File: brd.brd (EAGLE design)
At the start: 40.3 x 62.2 mm, 15 parts, among them IC1 OP27Z, X1 BNC-H, X2 BNC-H, X3 BNC-H, X4 BNC-H

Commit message: better circuit
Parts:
- added R5: 10K, resistor:0204V
- C2, C5: value (none) -> 10uF
- C3, C4: value (none) -> .1uF
- R1, R3: value (none) -> 10K
- R2: value (none) -> 50K
- moved R2 11.5 mm to (31.8, 76.2), turned to 180 degrees
- moved R3 4.58 mm to (25.4, 78.7), turned to 0 degrees
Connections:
- new net N$9: IC1.3, R2.2, R5.1
- net GND: now also R5.2; no longer IC1.3
- net N$1: no longer R2.2
- net N$3: no longer R3.1
- net N$6: now also R3.1; no longer R2.1
- net N$7: now also R2.1
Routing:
- net N$9: track 0.00 -> 24.1 mm
- net N$7: track 18.1 -> 36.1 mm
- net N$1: track 40.2 -> 29.2 mm
- net N$6: track 7.18 -> 16.5 mm
- net N$2: track 22.6 -> 15.3 mm
- net N$3: track 29.2 -> 23.9 mm
- net N$8: track 18.4 -> 22.9 mm
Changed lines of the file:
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@@
 <?xml version="1.0" encoding="utf-8"?>
 <!DOCTYPE eagle SYSTEM "eagle.dtd">
-<eagle version="7.5.0">
+<eagle version="8.1.0">
 <drawing>
 <settings>
@@
 </element>
 <element name="JP1" library="pinhead" package="1X03" value="" x="35.56" y="63.5" rot="R270"/>
-<element name="R1" library="resistor" package="0204V" value="" x="17.78" y="64.77" rot="R270"/>
-<element name="R2" library="resistor" package="0204V" value="" x="20.32" y="77.47"/>
-<element name="R3" library="resistor" package="0204V" value="" x="29.21" y="76.2" rot="R90"/>
+<element name="R1" library="resistor" package="0204V" value="10K" x="17.78" y="64.77" rot="R270"/>
+<element name="R2" library="resistor" package="0204V" value="50K" x="31.75" y="76.2" rot="R180"/>
+<element name="R3" library="resistor" package="0204V" value="10K" x="25.4" y="78.74"/>
 <element name="R4" library="resistor" package="0204V" value="" x="24.13" y="40.64" rot="R90"/>
 <element name="C1" library="resistor" package="C025-024X044" value="" x="25.4" y="34.29"/>
-<element name="C2" library="resistor" package="C025-024X044" value="" x="22.86" y="55.88" rot="R90"/>
-<element name="C3" library="resistor" package="C025-024X044" value="" x="26.67" y="55.88" rot="R90"/>
-<element name="C4" library="resistor" package="C025-024X044" value="" x="20.32" y="72.39" rot="R90"/>
-<element name="C5" library="resistor" package="C025-024X044" value="" x="24.13" y="72.39" rot="R90"/>
+<element name="C2" library="resistor" package="C025-024X044" value="10uF" x="22.86" y="55.88" rot="R90"/>
+<element name="C3" library="resistor" package="C025-024X044" value=".1uF" x="26.67" y="55.88" rot="R90"/>
+<element name="C4" library="resistor" package="C025-024X044" value=".1uF" x="20.32" y="72.39" rot="R90"/>
+<element name="C5" library="resistor" package="C025-024X044" value="10uF" x="24.13" y="72.39" rot="R90"/>
+<element name="R5" library="resistor" package="0204V" value="10K" x="36.83" y="72.39"/>
 </elements>
 <signals>
 <signal name="GND">
-<contactref element="IC1" pad="3"/>
 <contactref element="X1" pad="2"/>
 <contactref element="X3" pad="2"/>
@@
 <vertex x="0" y="19.05"/>
 </polygon>
+<contactref element="R5" pad="2"/>
 </signal>
 <signal name="N$1">
 <contactref element="IC1" pad="2"/>
+<contactref element="R1" pad="1"/>
 <contactref element="R3" pad="2"/>
-<contactref element="R1" pad="1"/>
-<contactref element="R2" pad="2"/>
-<wire x1="21.59" y1="77.47" x2="29.21" y2="77.47" width="0.4064" layer="16"/>
-<wire x1="17.78" y1="66.04" x2="19.05" y2="66.04" width="0.4064" layer="16"/>
-<wire x1="19.05" y1="66.04" x2="26.67" y2="66.04" width="0.4064" layer="16"/>
-<wire x1="26.67" y1="66.04" x2="26.67" y2="68.58" width="0.4064" layer="16"/>
-<wire x1="29.21" y1="77.47" x2="24.13" y2="77.47" width="0.4064" layer="16"/>
-<wire x1="24.13" y1="77.47" x2="22.86" y2="76.2" width="0.4064" layer="16"/>
-<wire x1="22.86" y1="76.2" x2="20.32" y2="76.2" width="0.4064" layer="16"/>
-<wire x1="20.32" y1="76.2" x2="17.78" y2="73.66" width="0.4064" layer="16"/>
-<wire x1="17.78" y1="73.66" x2="17.78" y2="68.58" width="0.4064" layer="16"/>
-<wire x1="17.78" y1="68.58" x2="19.05" y2="67.31" width="0.4064" layer="16"/>
-<wire x1="19.05" y1="67.31" x2="19.05" y2="66.04" width="0.4064" layer="16"/>
+<wire x1="26.67" y1="76.2" x2="26.67" y2="78.74" width="0.4064" layer="16"/>
+<wire x1="26.67" y1="76.2" x2="26.67" y2="68.58" width="0.4064" layer="16"/>
+<wire x1="17.78" y1="66.04" x2="17.78" y2="76.2" width="0.4064" layer="16"/>
+<wire x1="17.78" y1="76.2" x2="26.67" y2="76.2" width="0.4064" layer="16"/>
 </signal>
 <signal name="N$2">
@@
 <contactref element="R1" pad="2"/>
 <contactref element="X2" pad="1"/>
-<wire x1="17.78" y1="63.5" x2="13.97" y2="63.5" width="0.4064" layer="16"/>
-<wire x1="13.97" y1="63.5" x2="13.97" y2="57.15" width="0.4064" layer="16"/>
-<wire x1="17.78" y1="63.5" x2="17.78" y2="58.42" width="0.4064" layer="16"/>
-<wire x1="17.78" y1="58.42" x2="21.59" y2="58.42" width="0.4064" layer="16"/>
-<wire x1="21.59" y1="58.42" x2="24.13" y2="60.96" width="0.4064" layer="16"/>
+<wire x1="13.97" y1="57.15" x2="13.97" y2="59.69" width="0.4064" layer="16"/>
+<wire x1="13.97" y1="59.69" x2="17.78" y2="63.5" width="0.4064" layer="16"/>
+<wire x1="17.78" y1="63.5" x2="21.59" y2="63.5" width="0.4064" layer="16"/>
+<wire x1="21.59" y1="63.5" x2="24.13" y2="60.96" width="0.4064" layer="16"/>
 </signal>
 <signal name="N$3">
@@
 <contactref element="C4" pad="1"/>
 <contactref element="C5" pad="1"/>
-<contactref element="R3" pad="1"/>
+<wire x1="35.56" y1="66.04" x2="21.59" y2="66.04" width="0.4064" layer="16"/>
+<wire x1="21.59" y1="66.04" x2="21.59" y2="68.58" width="0.4064" layer="16"/>
 <wire x1="21.59" y1="68.58" x2="20.32" y2="68.58" width="0.4064" layer="16"/>
 <wire x1="20.32" y1="68.58" x2="20.32" y2="71.12" width="0.4064" layer="16"/>
-<wire x1="21.59" y1="68.58" x2="22.86" y2="68.58" width="0.4064" layer="16"/>
-<wire x1="22.86" y1="68.58" x2="22.86" y2="71.12" width="0.4064" layer="16"/>
-<wire x1="24.13" y1="71.12" x2="29.21" y2="71.12" width="0.4064" layer="16"/>
-<wire x1="29.21" y1="71.12" x2="35.56" y2="71.12" width="0.4064" layer="16"/>
-<wire x1="35.56" y1="71.12" x2="35.56" y2="66.04" width="0.4064" layer="16"/>
-<wire x1="24.13" y1="71.12" x2="22.86" y2="71.12" width="0.4064" layer="16"/>
-<wire x1="29.21" y1="74.93" x2="29.21" y2="71.12" width="0.4064" layer="16"/>
-</signal>
-<signal name="N$6">
-<contactref element="X1" pad="1"/>
-<contactref element="R2" pad="1"/>
-<wire x1="13.97" y1="72.39" x2="19.05" y2="77.47" width="0.4064" layer="16"/>
+<wire x1="21.59" y1="68.58" x2="24.13" y2="71.12" width="0.4064" layer="16"/>
 </signal>
 <signal name="N$7">
@@
 <contactref element="C2" pad="2"/>
 <contactref element="C3" pad="2"/>
-<wire x1="35.56" y1="60.96" x2="31.75" y2="57.15" width="0.4064" layer="16"/>
-<wire x1="31.75" y1="57.15" x2="26.67" y2="57.15" width="0.4064" layer="16"/>
-<wire x1="22.86" y1="57.15" x2="26.67" y2="57.15" width="0.4064" layer="16"/>
+<contactref element="R2" pad="1"/>
+<wire x1="36.6268" y1="72.8318875" x2="36.0018875" y2="73.4568" width="0.4064" layer="16"/>
+<wire x1="35.56" y1="61.08563125" x2="35.56" y2="60.96" width="0.4064" layer="16"/>
+<wire x1="36.0018875" y1="73.4568" x2="35.7632" y2="73.4568" width="0.4064" layer="16"/>
+<wire x1="35.56" y1="61.08563125" x2="37.4904" y2="63.01603125" width="0.4064" layer="16"/>
+<wire x1="35.7632" y1="73.4568" x2="33.02" y2="76.2" width="0.4064" layer="16"/>
+<wire x1="37.4904" y1="66.52396875" x2="36.6268" y2="67.38756875" width="0.4064" layer="16"/>
+<wire x1="36.6268" y1="67.38756875" x2="36.6268" y2="72.8318875" width="0.4064" layer="16"/>
+<wire x1="37.4904" y1="63.01603125" x2="37.4904" y2="66.52396875" width="0.4064" layer="16"/>
+<wire x1="35.56" y1="60.96" x2="33.02" y2="60.96" width="0.4064" layer="16"/>
+<wire x1="33.02" y1="60.96" x2="30.48" y2="58.42" width="0.4064" layer="16"/>
+<wire x1="30.48" y1="58.42" x2="27.94" y2="58.42" width="0.4064" layer="16"/>
+<wire x1="27.94" y1="58.42" x2="26.67" y2="57.15" width="0.4064" layer="16"/>
+<wire x1="26.67" y1="57.15" x2="22.86" y2="57.15" width="0.4064" layer="16"/>
 <wire x1="26.67" y1="57.15" x2="26.67" y2="60.96" width="0.4064" layer="16"/>
 </signal>
@@
 <contactref element="X4" pad="1"/>
 <wire x1="24.13" y1="39.37" x2="24.13" y2="34.29" width="0.4064" layer="16"/>
-<wire x1="24.13" y1="34.29" x2="21.59" y2="34.29" width="0.4064" layer="16"/>
-<wire x1="21.59" y1="34.29" x2="13.97" y2="26.67" width="0.4064" layer="16"/>
+<wire x1="19.05" y1="34.29" x2="19.05" y2="26.67" width="0.4064" layer="16"/>
+<wire x1="19.05" y1="26.67" x2="13.97" y2="26.67" width="0.4064" layer="16"/>
+<wire x1="24.13" y1="34.29" x2="19.05" y2="34.29" width="0.4064" layer="16"/>
+</signal>
+<signal name="N$9">
+<contactref element="IC1" pad="3"/>
+<contactref element="R5" pad="1"/>
+<contactref element="R2" pad="2"/>
+<wire x1="24.13" y1="68.58" x2="24.13" y2="67.31" width="0.4064" layer="16"/>
+<wire x1="24.13" y1="67.31" x2="33.02" y2="67.31" width="0.4064" layer="16"/>
+<wire x1="33.02" y1="72.39" x2="33.02" y2="67.31" width="0.4064" layer="16"/>
+<wire x1="33.02" y1="72.39" x2="35.56" y2="72.39" width="0.4064" layer="16"/>
+<wire x1="30.48" y1="76.2" x2="30.48" y2="72.39" width="0.4064" layer="16"/>
+<wire x1="30.48" y1="72.39" x2="33.02" y2="72.39" width="0.4064" layer="16"/>
+</signal>
+<signal name="N$6">
+<contactref element="X1" pad="1"/>
+<contactref element="R3" pad="1"/>
+<wire x1="13.97" y1="72.39" x2="13.97" y2="78.74" width="0.4064" layer="16"/>
+<wire x1="13.97" y1="78.74" x2="24.13" y2="78.74" width="0.4064" layer="16"/>
 </signal>
 </signals>

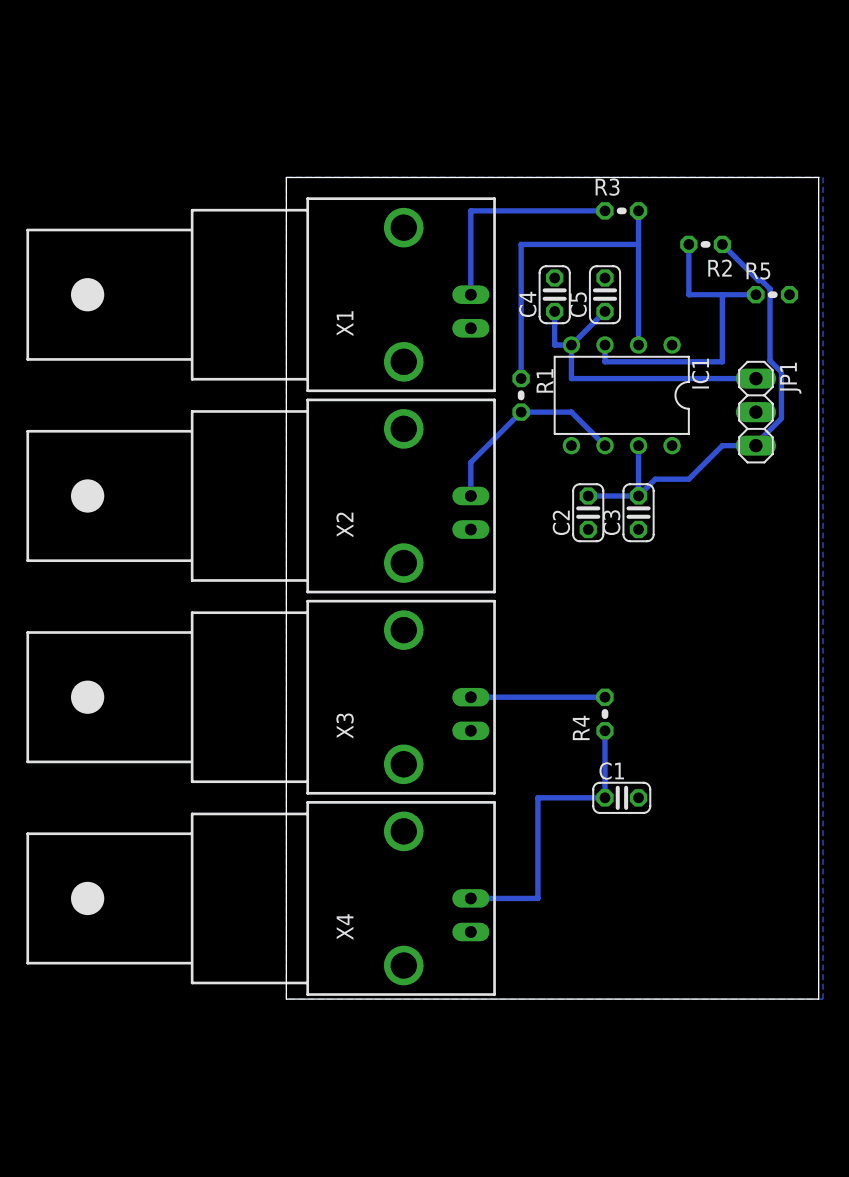
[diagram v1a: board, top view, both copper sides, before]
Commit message: added switches
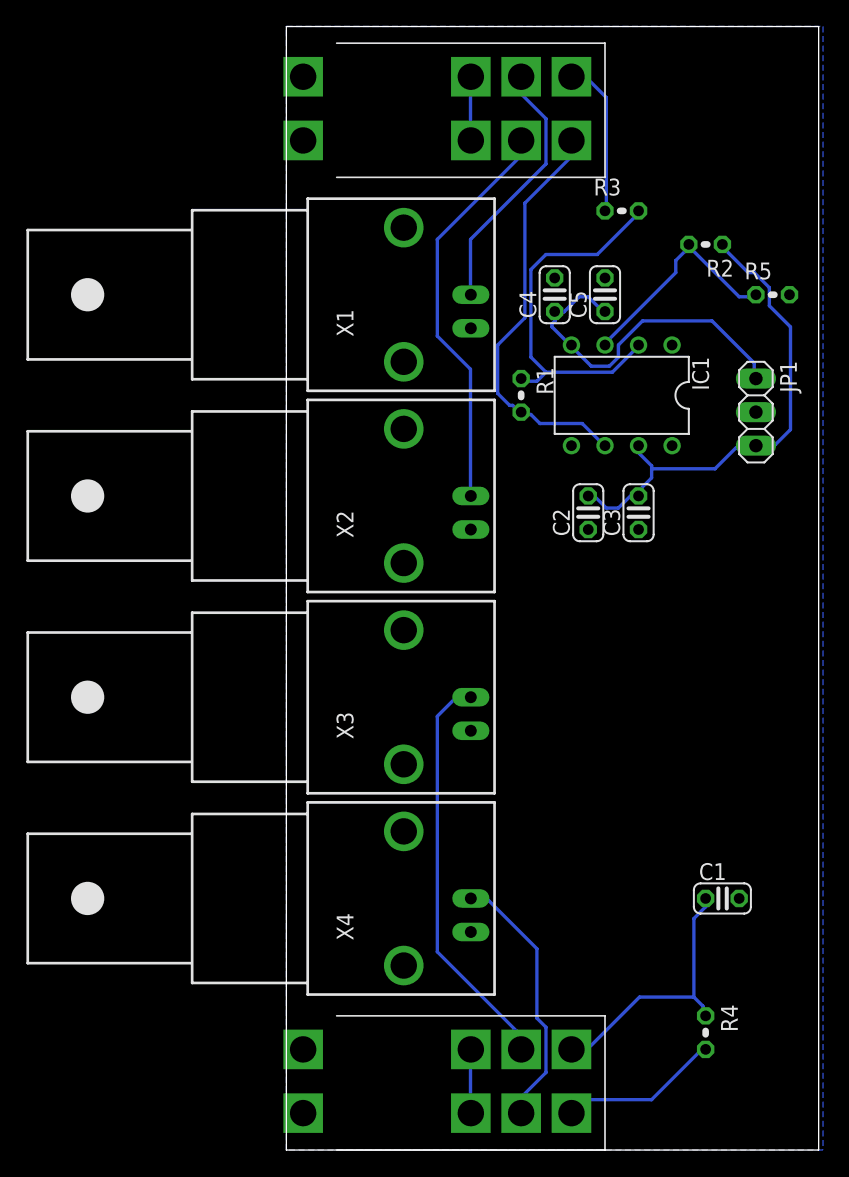
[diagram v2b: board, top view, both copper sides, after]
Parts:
- added U$1, U$2: DP3T-TOGGLE, switch-jqi:7201MD9AV2BE
- moved R4 25.3 mm to (31.8, 16.5), turned to 270 degrees
- moved C1 10.8 mm to (33.0, 26.7)
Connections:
- new net N$10: U$2.1, U$2.4
- new net N$12: U$1.5, X2.1
- new net N$14: R3.1, U$1.3
- new net N$15: U$1.1, U$1.4
- new net N$16: R4.2, U$2.6
- new net N$4: U$2.2, X3.1
- net N$2: now also U$1.6; no longer X2.1
- net N$5: now also U$2.5, X4.1; no longer R4.2, X3.1
- net N$6: now also U$1.2; no longer R3.1
- net N$8: now also U$2.3; no longer X4.1
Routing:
- net N$4: track 0.00 -> 31.1 mm
- net N$12: track 0.00 -> 30.6 mm
- net N$2: track 15.3 -> 31.3 mm
- net N$16: track 0.00 -> 12.1 mm
- net N$14: track 0.00 -> 11.9 mm
- net N$5: track 10.2 -> 20.1 mm
- net N$9: track 24.1 -> 17.4 mm
- net N$15: track 0.00 -> 4.83 mm
- net N$10: track 0.00 -> 4.83 mm
- net N$3: track 23.9 -> 27.2 mm
- net N$6: track 16.5 -> 19.6 mm
- net N$8: track 22.9 -> 20.6 mm
- net N$7: track 36.1 -> 37.7 mm
- net N$1: track 29.2 -> 28.7 mm
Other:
- board size 40.3 x 62.2 mm -> 40.3 x 85.1 mm

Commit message: fixed ordering
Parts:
- moved X3 15.2 mm to (8.89, 26.7)
- moved X4 15.2 mm to (8.89, 41.9)
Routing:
- net N$4: track 31.1 -> 13.7 mm
- net N$5: track 20.1 -> 35.3 mm
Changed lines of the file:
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@@
 <attribute name="DIGIKEY" value="A32260-ND" x="8.89" y="57.15" size="1.778" layer="27" rot="R90" display="off"/>
 </element>
-<element name="X3" library="connector-jqi" package="BNC90" value="BNC-H" x="8.89" y="41.91" rot="R90">
+<element name="X3" library="connector-jqi" package="BNC90" value="BNC-H" x="8.89" y="26.67" rot="R90">
+<attribute name="DIGIKEY" value="A32260-ND" x="8.89" y="26.67" size="1.778" layer="27" rot="R90" display="off"/>
+</element>
+<element name="X4" library="connector-jqi" package="BNC90" value="BNC-H" x="8.89" y="41.91" rot="R90">
 <attribute name="DIGIKEY" value="A32260-ND" x="8.89" y="41.91" size="1.778" layer="27" rot="R90" display="off"/>
-</element>
-<element name="X4" library="connector-jqi" package="BNC90" value="BNC-H" x="8.89" y="26.67" rot="R90">
-<attribute name="DIGIKEY" value="A32260-ND" x="8.89" y="26.67" size="1.778" layer="27" rot="R90" display="off"/>
 </element>
 <element name="JP1" library="pinhead" package="1X03" value="" x="35.56" y="63.5" rot="R270"/>
@@
 <contactref element="U$2" pad="5"/>
 <contactref element="X4" pad="1"/>
-<wire x1="15.3162" y1="26.5176" x2="14.1732" y2="26.5176" width="0.254" layer="16"/>
-<wire x1="18.9738" y1="22.86" x2="15.3162" y2="26.5176" width="0.254" layer="16"/>
-<wire x1="18.9738" y1="17.6022" x2="18.9738" y2="22.86" width="0.254" layer="16"/>
+<wire x1="15.3162" y1="41.8338" x2="14.1732" y2="41.8338" width="0.254" layer="16"/>
+<wire x1="18.9738" y1="38.1762" x2="15.3162" y2="41.8338" width="0.254" layer="16"/>
+<wire x1="18.9738" y1="17.6022" x2="18.9738" y2="38.1762" width="0.254" layer="16"/>
 <wire x1="19.6596" y1="16.9164" x2="18.9738" y2="17.6022" width="0.254" layer="16"/>
 <wire x1="19.6596" y1="13.4874" x2="19.6596" y2="16.9164" width="0.254" layer="16"/>
 <wire x1="17.8308" y1="11.6586" x2="19.6596" y2="13.4874" width="0.254" layer="16"/>
 <wire x1="17.8308" y1="10.5156" x2="17.8308" y2="11.6586" width="0.254" layer="16"/>
-<wire x1="14.1732" y1="26.5176" x2="13.97" y2="26.67" width="0.254" layer="16"/>
+<wire x1="14.1732" y1="41.8338" x2="13.97" y2="41.91" width="0.254" layer="16"/>
 <wire x1="17.8308" y1="10.5156" x2="17.78" y2="10.414" width="0.254" layer="16"/>
 </signal>
@@
 <contactref element="X3" pad="1"/>
 <contactref element="U$2" pad="2"/>
-<wire x1="12.8016" y1="41.8338" x2="13.9446" y2="41.8338" width="0.254" layer="16"/>
-<wire x1="11.43" y1="40.4622" x2="12.8016" y2="41.8338" width="0.254" layer="16"/>
-<wire x1="11.43" y1="22.6314" x2="11.43" y2="40.4622" width="0.254" layer="16"/>
-<wire x1="17.6022" y1="16.4592" x2="11.43" y2="22.6314" width="0.254" layer="16"/>
-<wire x1="17.6022" y1="15.3162" x2="17.6022" y2="16.4592" width="0.254" layer="16"/>
-<wire x1="13.9446" y1="41.8338" x2="13.97" y2="41.91" width="0.254" layer="16"/>
+<wire x1="15.3162" y1="26.5176" x2="14.1732" y2="26.5176" width="0.254" layer="16"/>
+<wire x1="16.6878" y1="25.146" x2="15.3162" y2="26.5176" width="0.254" layer="16"/>
+<wire x1="16.6878" y1="16.2306" x2="16.6878" y2="25.146" width="0.254" layer="16"/>
+<wire x1="17.6022" y1="15.3162" x2="16.6878" y2="16.2306" width="0.254" layer="16"/>
+<wire x1="14.1732" y1="26.5176" x2="13.97" y2="26.67" width="0.254" layer="16"/>
 <wire x1="17.6022" y1="15.3162" x2="17.78" y2="15.24" width="0.254" layer="16"/>
 </signal>
